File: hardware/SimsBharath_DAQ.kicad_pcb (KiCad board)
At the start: 2 copper layers, 70 x 115 mm, 95 parts, among them IC2 MIC37100-3.3WS, IC3 LAN8742A-CZ-TR, J1 Conn_02x05_Odd_Even, J10 702471052, J11 702471052, J2 USB1030-GF-P-B-B, J3 702471052, J4 702471052, J5 702471052, J6 702471052, J7 702471052, J8 702471052, J9 1-406507-5, T1 H1102NL, U1 STM32H753ZIT6, Y1 XRCGB25M000F3A16R0, Y2 XRCGB25M000F3A16R0, Y3 CM7V-T1A-32.768KHZ-7PF-20PPM-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

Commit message: updated
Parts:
- added +3.3V1: TestPoint, TestPoint:TestPoint_Pad_D1.5mm, F.Cu at (198.1, 64.3)
- added +5V1: TestPoint, TestPoint:TestPoint_Pad_D1.5mm, F.Cu at (195.2, 47.6)
- added C38: 1uF, Murata:GRM18x, F.Cu at (177.9, 102.5)
- added C39: 1uF, Murata:GRM18x, F.Cu at (177.9, 106.5)
- added C40: 0.1uF, Murata:GRM18x, F.Cu at (212.1, 126.9)
- added R36: 20k, Murata:RESC1608X95N, F.Cu at (177.8, 100.5)
- added R37: 20k, Murata:RESC1608X95N, F.Cu at (177.8, 104.5)
- added R38: 10k, Murata:RESC1608X95N, F.Cu at (208.5, 60.3)
- added R39: 10k, Murata:RESC1608X95N, F.Cu at (208.5, 63.0)
- added SW1: SW_Push, Button_Switch_THT:SW_PUSH_6mm_H4.3mm, F.Cu at (212.0, 131.7)
- C1, C25, C26, C29, C30, C31, C34, C36, L1, R1, R13, R14, R33, R34, R35, R4: moved to B.Cu
- R3: value 10k -> 0E
- X3: renamed from Y3; moved to B.Cu
- moved R33 107.3 mm to (204.3, 79.5), turned to 90 degrees
- moved C36 106.5 mm to (202.2, 79.5), turned to 90 degrees
- moved C34 99.3 mm to (193.8, 79.5), turned to 90 degrees
- moved R34 94.5 mm to (191.7, 79.5), turned to 90 degrees
- moved R32 82.1 mm to (180.0, 39.1)
- moved C1 78.3 mm to (183.6, 96.8), turned to 180 degrees
- moved D3 78.2 mm to (180.0, 37.1)
- moved C2 77.3 mm to (183.7, 96.8)
- moved C28 76.0 mm to (203.9, 108.9)
- moved C27 75.6 mm to (204.0, 104.1)
- moved C25 72.8 mm to (198.2, 108.3)
- moved R3 71.8 mm to (208.5, 57.6)
- moved C26 71.3 mm to (198.2, 106.3)
- moved R13 69.7 mm to (205.0, 121.4), turned to -90 degrees
- moved R4 69.4 mm to (201.7, 109.5), turned to 90 degrees
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- renumbered IC2 to U2, IC3 to U3, T1 to U4, Y1 to X1, Y2 to X2
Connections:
- net /CONNECTORS/~{nRST} renamed /MCU/~{NRST}
- net Net-(T1-RX+) renamed /CONNECTORS/RX P
- net Net-(T1-RX-) renamed /CONNECTORS/RX N
- net Net-(T1-TX+) renamed /CONNECTORS/TX P
- net Net-(T1-TX-) renamed /CONNECTORS/TX N
- J2 pad 1: /CONNECTORS/USB_FS_VBUS -> +5V
- J4 pad 1: /CONNECTORS/DAC1 -> /CONNECTORS/M_DAC0
- J4 pad 2: /CONNECTORS/DAC0 -> /CONNECTORS/M_DAC1
- R3 pad 1: Net-(IC1-PA9) -> VBAT
- R3 pad 2: +5V -> +3.3V
- U1 pad 143: unconnected-(IC1-PDR_ON-Pad143) -> Net-(U1-PDR_ON)
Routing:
- net Net-(U3-VDD1A): track 0.00 -> 60.7 mm, vias 0 -> 1
- net +3.3V: track 0.00 -> 55.3 mm, vias 0 -> 1
- net /CONNECTORS/RX P: track 0.00 -> 23.5 mm, vias 0 -> 1
- net /MCU/OSC32_OUT: track 0.00 -> 17.8 mm, vias 0 -> 1
- net /MCU/PH1-OSC_OUT: track 0.00 -> 15.3 mm
- net Net-(J9-Pad4): track 0.00 -> 15.3 mm
- net /CONNECTORS/TD-: track 0.00 -> 13.3 mm, vias 0 -> 2
- net /MCU/~{NRST}: track 0.00 -> 12.9 mm
- net /CONNECTORS/TX P: track 0.00 -> 12.8 mm
- net /CONNECTORS/TD+: track 0.00 -> 12.1 mm, vias 0 -> 2
- net Net-(J9-Pad7): track 0.00 -> 11.6 mm
- net /MCU/PHO-OSC_IN: track 0.00 -> 11.3 mm
- net /CONNECTORS/RD-: track 0.00 -> 11.0 mm
- net /CONNECTORS/RX N: track 0.00 -> 10.9 mm
- net /CONNECTORS/RD+: track 0.00 -> 10.6 mm
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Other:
- board text added: "3.3V LED"
- board text added: "5V LED"

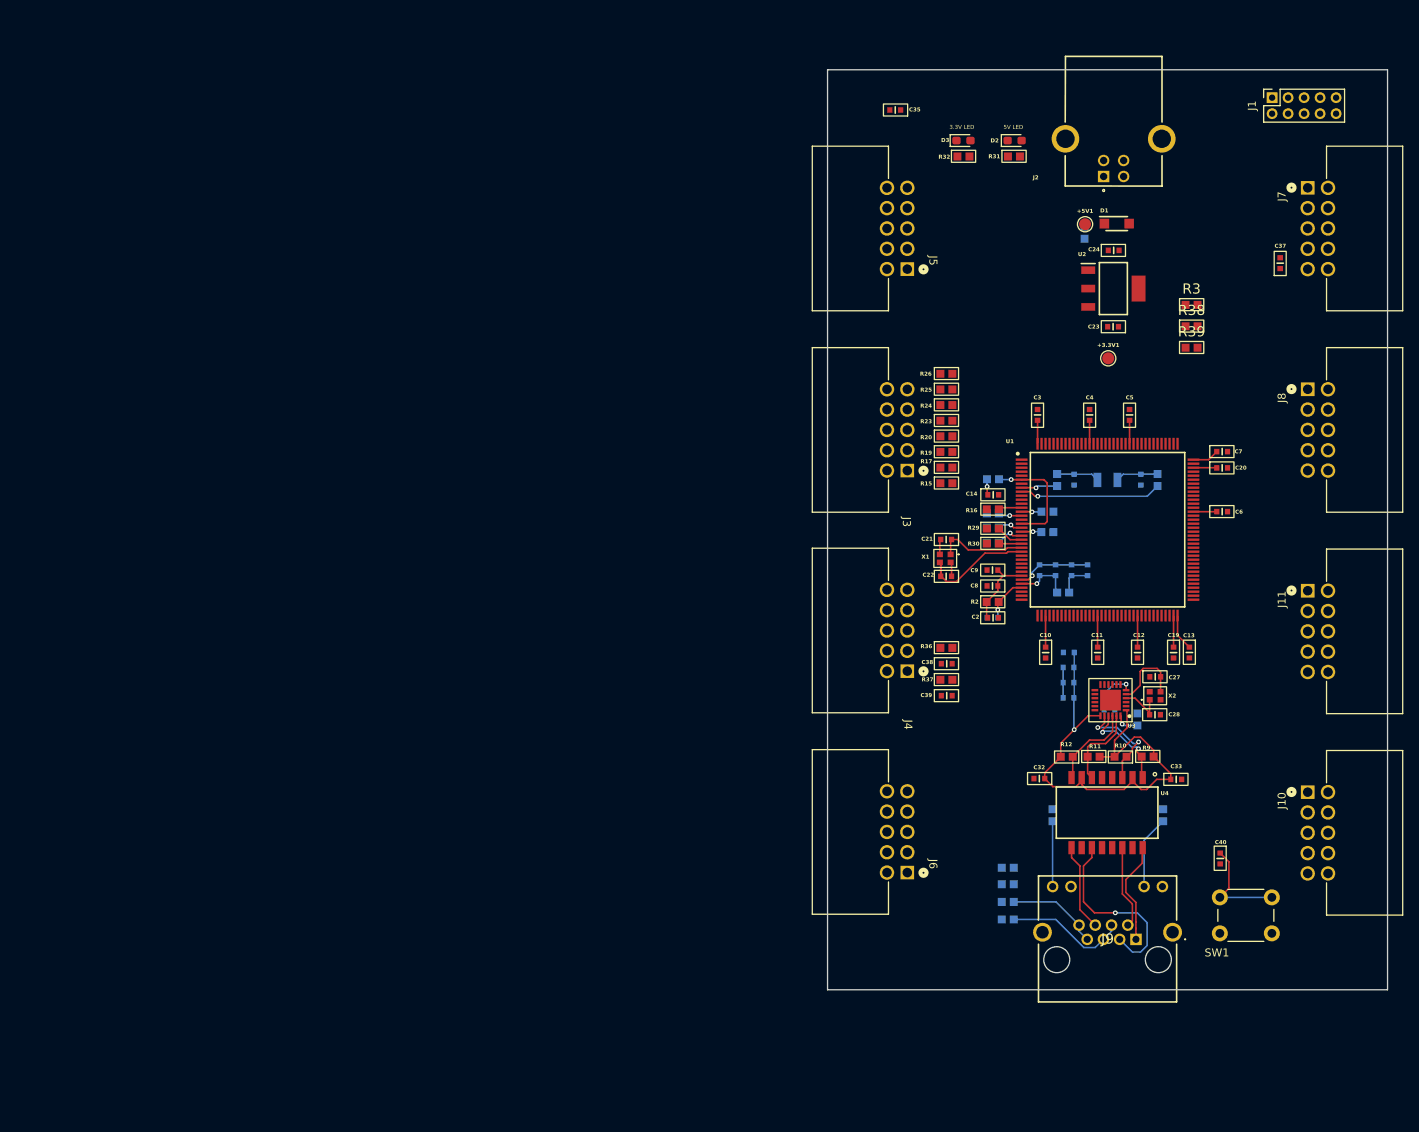
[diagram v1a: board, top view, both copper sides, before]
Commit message: In layout finalised Board Dimensions ...
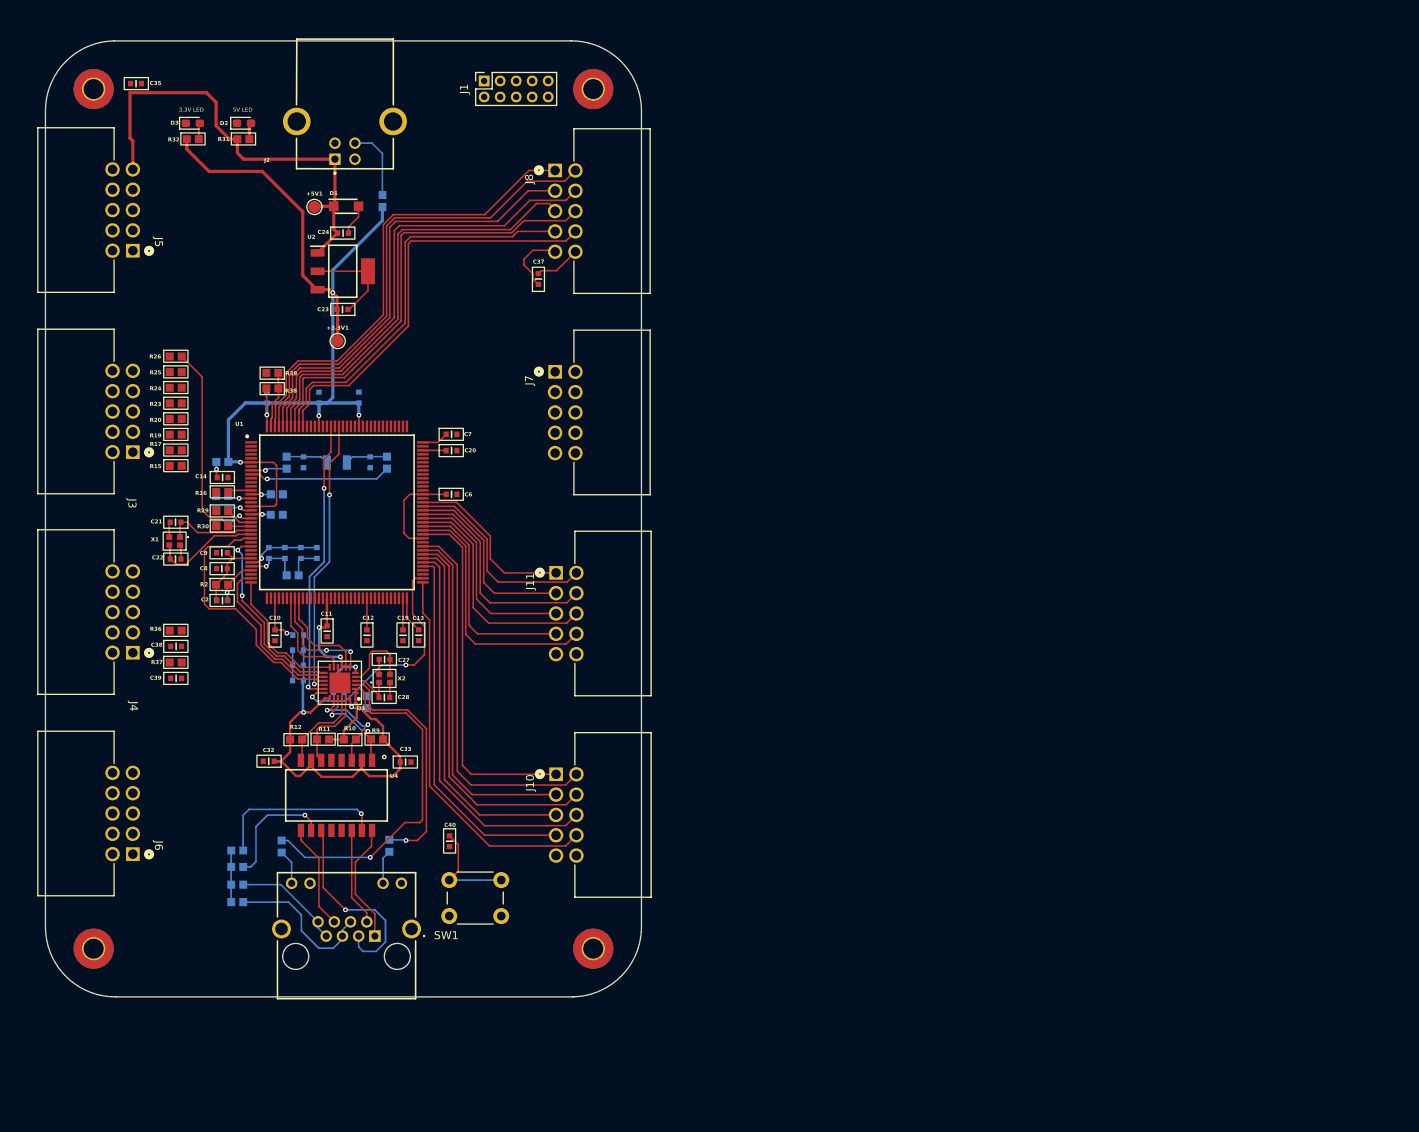
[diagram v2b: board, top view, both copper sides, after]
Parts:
- removed the R3 at (208.5, 57.6)
- added REF**: MountingHole_2.5mm_Pad_TopBottom, MountingHole:MountingHole_2.5mm_Pad_TopBottom, F.Cu at (133.7, 30.7)
- added REF**: MountingHole_2.5mm_Pad_TopBottom, MountingHole:MountingHole_2.5mm_Pad_TopBottom, F.Cu at (133.7, 138.1)
- added REF**: MountingHole_2.5mm_Pad_TopBottom, MountingHole:MountingHole_2.5mm_Pad_TopBottom, F.Cu at (71.3, 138.1)
- added REF**: MountingHole_2.5mm_Pad_TopBottom, MountingHole:MountingHole_2.5mm_Pad_TopBottom, F.Cu at (71.3, 30.7)
- C3, C4, C5: moved to B.Cu
- moved R38 115.2 mm to (93.6, 68.1), turned to 180 degrees
- moved R39 114.9 mm to (93.6, 66.2), turned to 180 degrees
- moved J1 98.5 mm to (120.1, 29.7)
- moved J8 98.0 mm to (128.9, 40.8)
- moved J7 96.8 mm to (128.9, 66.0)
- moved J3 96.8 mm to (76.2, 76.1)
- moved J4 96.8 mm to (76.2, 101.1)
- moved J5 96.8 mm to (76.2, 50.9)
- moved J6 96.8 mm to (76.2, 126.3)
- moved R13 96.8 mm to (108.2, 125.3)
- moved R14 96.4 mm to (94.8, 125.4)
- moved C11 96.4 mm to (100.4, 98.4)
- moved C1 96.3 mm to (87.3, 94.6)
- moved C24 96.3 mm to (102.4, 48.7)
- moved C25 96.3 mm to (101.9, 106.1)
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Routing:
- net +3.3V: track 55.3 -> 166.6 mm, vias 1 -> 8
- net +5V: track 0.00 -> 65.3 mm
- net /CONNECTORS/PB1: track 0.00 -> 60.0 mm
- net /CONNECTORS/PB0: track 0.00 -> 58.0 mm
- net /CONNECTORS/PB3: track 0.00 -> 57.6 mm
- net /CONNECTORS/PB2: track 0.00 -> 55.9 mm
- net /CONNECTORS/PB5: track 0.00 -> 55.4 mm
- net /CONNECTORS/PB4: track 0.00 -> 54.3 mm
- net /CONNECTORS/PB7: track 0.00 -> 52.4 mm
- net /CONNECTORS/PB6: track 0.00 -> 50.4 mm
- net /CONNECTORS/PD5: track 0.00 -> 49.0 mm
- net /CONNECTORS/PD3: track 0.00 -> 48.1 mm
- net /CONNECTORS/PD7: track 0.00 -> 47.8 mm
- net /CONNECTORS/PD1: track 0.00 -> 47.2 mm
- net /CONNECTORS/PD6: track 0.00 -> 46.5 mm
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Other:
- board size 70 x 115 mm -> 74.5 x 119.5 mm

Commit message: completed the design
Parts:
- C14, C37, R15, R17, R19, R20, R23, R24, R25, R26: moved to B.Cu
- R18, R21, R22, R27, R28: moved to F.Cu
- moved R18 21.9 mm to (80.6, 64.2), turned to 0 degrees
- moved R16 20.7 mm to (80.6, 61.4)
- moved R27 17.8 mm to (80.6, 72.3), turned to 0 degrees
- moved R15 16.4 mm to (80.6, 61.4)
- moved R26 16.3 mm to (80.6, 80.4)
- moved R21 16.1 mm to (80.6, 66.9)
- moved R22 15.3 mm to (80.6, 69.6)
- moved R28 12.2 mm to (80.6, 75.0)
- moved R17 11.7 mm to (80.6, 64.1)
- moved R25 11.7 mm to (80.6, 77.7)
- moved R29 8.80 mm to (80.6, 77.7)
- moved R30 8.28 mm to (80.6, 80.4)
- moved C40 7.11 mm to (115.8, 131.8)
- moved R24 7.05 mm to (80.6, 75.0)
- moved R19 7.03 mm to (80.6, 66.9)
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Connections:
- net /CONNECTORS/USB_FS_DM renamed /CONNECTORS/USB_FS_D N
- net /CONNECTORS/USB_FS_DP renamed /CONNECTORS/USB_FS_D P
- J3 pad 1: /CONNECTORS/ADC3_1 -> /CONNECTORS/ADC3_8
- J3 pad 2: /CONNECTORS/ADC3_2 -> /CONNECTORS/ADC3_7
- J3 pad 3: /CONNECTORS/ADC3_3 -> /CONNECTORS/ADC3_6
- J3 pad 4: /CONNECTORS/ADC3_4 -> /CONNECTORS/ADC3_5
- J3 pad 5: /CONNECTORS/ADC3_5 -> /CONNECTORS/ADC3_4
- J3 pad 6: /CONNECTORS/ADC3_6 -> /CONNECTORS/ADC3_3
- J3 pad 7: /CONNECTORS/ADC3_7 -> /CONNECTORS/ADC3_2
- J3 pad 8: /CONNECTORS/ADC3_8 -> /CONNECTORS/ADC3_1
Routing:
- net GND: track 46.0 -> 335.3 mm, vias 0 -> 328
- net +5V: track 65.3 -> 269.7 mm, vias 0 -> 1
- net +3.3V: track 166.6 -> 274.7 mm, vias 8 -> 14
- net /CONNECTORS/USB_FS_D N: track 0.00 -> 104.0 mm
- net /CONNECTORS/USB_FS_D P: track 9.17 -> 108.0 mm
- net /CONNECTORS/UART1_RX: track 0.00 -> 75.4 mm, vias 0 -> 1
- net /CONNECTORS/UART2_RX: track 0.00 -> 75.2 mm, vias 0 -> 1
- net /CONNECTORS/I2C2_SDA: track 0.00 -> 74.9 mm, vias 0 -> 1
- net /CONNECTORS/I2C2_SCL: track 0.00 -> 73.1 mm, vias 0 -> 1
- net /CONNECTORS/I2C1_SDA: track 0.00 -> 69.5 mm, vias 0 -> 1
- net /CONNECTORS/UART1_TX: track 0.85 -> 69.9 mm, vias 0 -> 1
- net /CONNECTORS/UART2_TX: track 0.00 -> 67.9 mm, vias 0 -> 1
- net /CONNECTORS/I2C1_SCL: track 0.00 -> 64.4 mm, vias 0 -> 1
- net /CONNECTORS/SPI5_SCK: track 0.00 -> 63.6 mm, vias 0 -> 2
- net /CONNECTORS/SPI5_MISO: track 0.00 -> 63.0 mm, vias 0 -> 2
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- added copper zone on B.Cu, net GND
- added copper zone on F.Cu, net GND

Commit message: completed the design with perfect mechanics
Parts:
- removed the REF** at (133.7, 30.7)
- removed the REF** at (133.7, 138.1)
- removed the REF** at (71.3, 138.1)
- removed the REF** at (71.3, 30.7)
- added J12: Conn_01x03, Connector_PinHeader_2.54mm:PinHeader_1x03_P2.54mm_Vertical, F.Cu at (144.2, 50.0)
- added REF**: MountingHole_2.5mm_Pad_TopBottom, MountingHole:MountingHole_2.5mm_Pad_TopBottom, F.Cu at (162.0, 150.5)
- added REF**: MountingHole_2.5mm_Pad_TopBottom, MountingHole:MountingHole_2.5mm_Pad_TopBottom, F.Cu at (100.0, 43.5)
- added REF**: MountingHole_2.5mm_Pad_TopBottom, MountingHole:MountingHole_2.5mm_Pad_TopBottom, F.Cu at (100.0, 150.5)
- added REF**: MountingHole_2.5mm_Pad_TopBottom, MountingHole:MountingHole_2.5mm_Pad_TopBottom, F.Cu at (162.0, 43.5)
- moved J3 31.5 mm to (102.2, 89.2)
- moved J4 31.5 mm to (102.2, 114.2)
- moved J5 31.5 mm to (102.2, 64.0)
- moved J6 31.5 mm to (102.2, 139.4)
- moved C11 31.5 mm to (129.5, 110.6)
- moved C25 31.5 mm to (130.9, 118.3)
- moved C6 31.5 mm to (145.0, 93.5)
- moved C7 31.5 mm to (145.0, 86.0)
- moved C8 31.5 mm to (116.3, 102.8)
- moved D3 31.5 mm to (112.7, 47.1)
- moved U3 31.5 mm to (131.1, 117.1)
- moved C1 31.5 mm to (116.3, 106.8)
- moved C20 31.5 mm to (145.0, 88.0)
- moved C24 31.5 mm to (131.5, 60.8)
- moved R4 31.5 mm to (134.4, 119.5)
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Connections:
- J1 pad 1: +3.3V -> /CONNECTORS/+5V-JTAG
- J2 pad 1: +5V -> /CONNECTORS/+5V-USB
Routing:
- net GND: track 335.3 -> 382.2 mm, vias 328 -> 316
- net +3.3V: track 274.7 -> 236.3 mm
- net VCAP: track 6.88 -> 39.4 mm, vias 0 -> 2
- net /CONNECTORS/+5V-USB: track 0.00 -> 18.6 mm, vias 0 -> 1
- net /CONNECTORS/+5V-JTAG: track 0.00 -> 16.2 mm, vias 0 -> 1
- net +5V: track 269.7 -> 282.5 mm
- net Net-(J9-Pad7): track 16.4 -> 13.6 mm, vias 1 -> 0
- net /CONNECTORS/RX P: track 28.6 -> 26.0 mm
- net /CONNECTORS/UART1_RX: track 75.4 -> 76.8 mm
- net Net-(J9-A_GREEN_2): track 7.75 -> 6.37 mm
- net /CONNECTORS/I2C2_SCL: track 73.1 -> 74.4 mm
- net /CONNECTORS/USB_FS_D P: track 108.0 -> 106.7 mm
- net /CONNECTORS/UART2_TX: track 67.9 -> 69.0 mm
- net /CONNECTORS/ADC3_2: track 8.15 -> 9.22 mm
- net /CONNECTORS/ADC3_1: track 14.1 -> 15.2 mm
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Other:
- board size 74.5 x 119.5 mm -> 74 x 119 mm
